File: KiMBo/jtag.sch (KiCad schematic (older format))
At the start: 9 parts, among them U1 OSD3358, Y2 6K30032768K0702070401, Y3 7A-24.000MAAJ-T

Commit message: Create more footprints and add more associations
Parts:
- Y3: footprint (none) -> KiMBo:Crystal_SMD_7A_2Pads
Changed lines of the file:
@@
 F 0 "Y3" V 4800 4150 50  0000 C CNN
 F 1 "7A-24.000MAAJ-T" V 4375 3875 50  0000 C CNN
-F 2 "" H 4700 4000 50  0001 C CNN
+F 2 "KiMBo:Crystal_SMD_7A_2Pads" H 4700 4000 50  0001 C CNN
 F 3 "" H 4700 4000 50  0000 C CNN
 	1    4700 4000

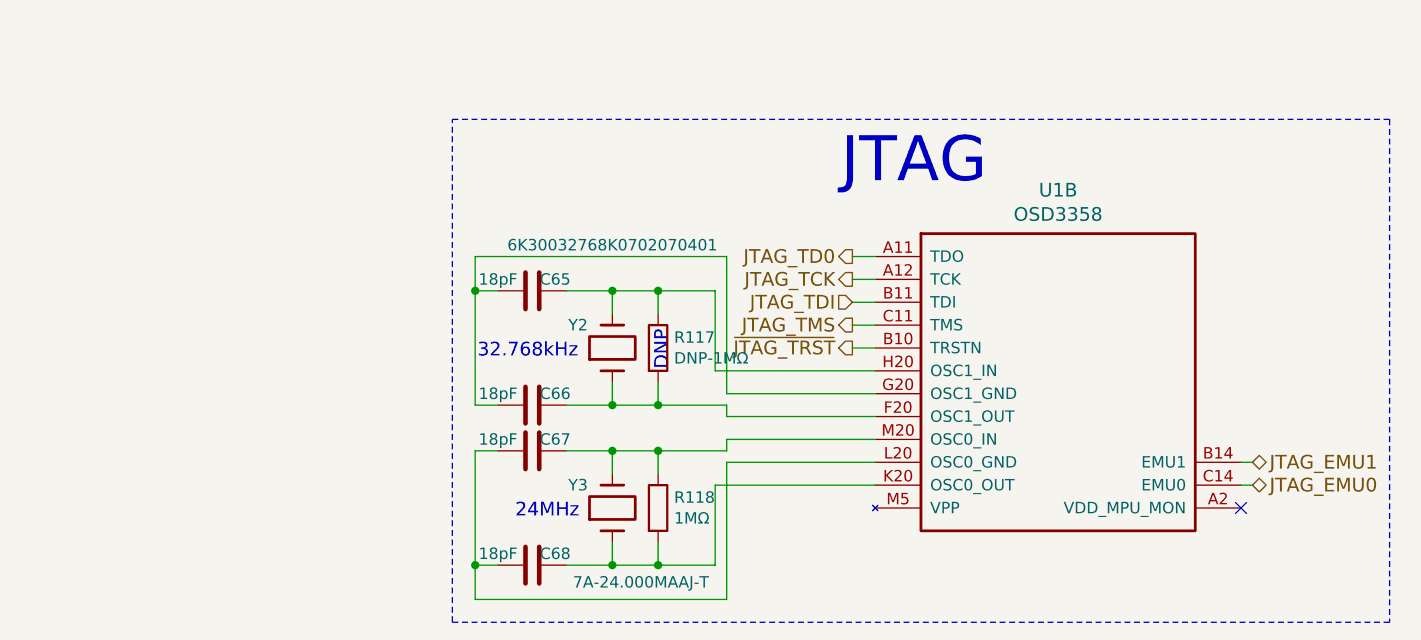
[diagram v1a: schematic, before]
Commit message: Complete footprint association
Next step is layout, adjustments may need to be made to the schematic at a later point.
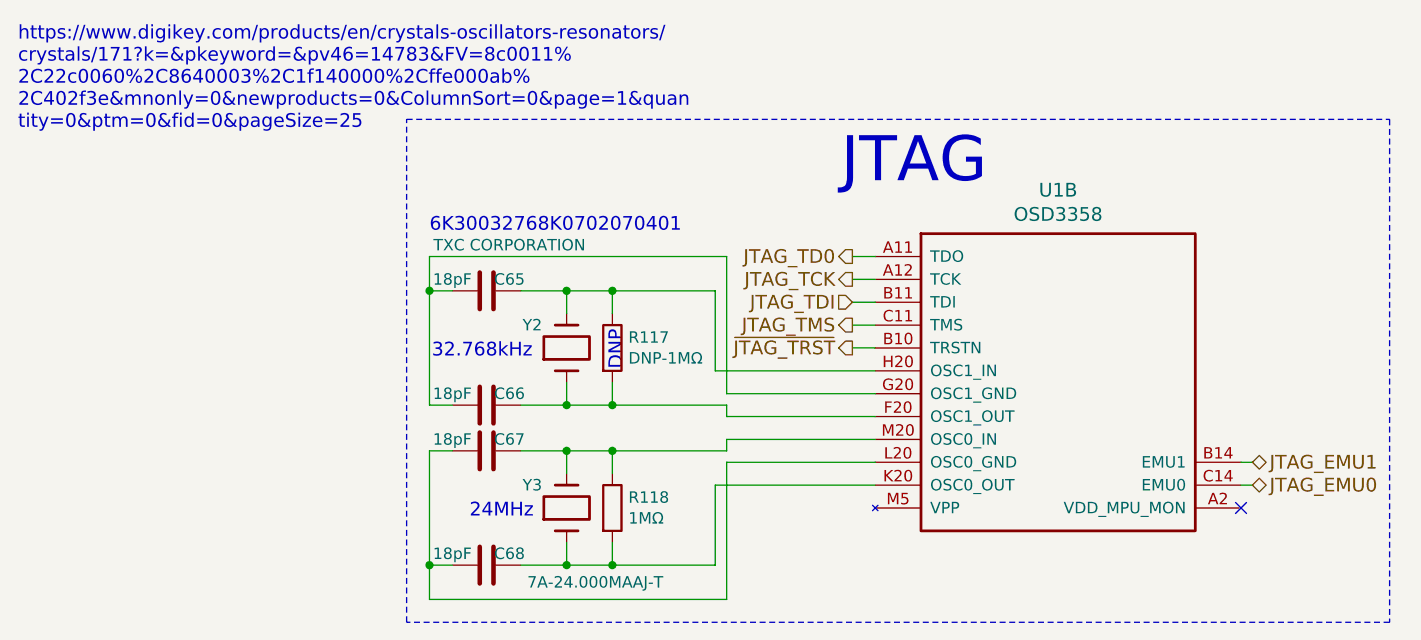
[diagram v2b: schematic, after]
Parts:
- R117: footprint (none) -> Resistors_SMD:R_0603
- Y2: value 6K30032768K0702070401 -> TXC CORPORATION; footprint (none) -> KiMBo:Crystal_SMD_32.768kHz_2Pads
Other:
- note added: "6K30032768K0702070401"
- note added: "https://www.digikey.com/products/en/crystals-oscillators-resonators/\ncrystals/171?k=&pkeyword=&pv46=14783&FV=8c0011%\n2C22c0060%2C8640003%2C1f140000%2Cffe000ab%\n2C402f3e&mnonly=0&newproducts=0&ColumnSort=0&page=1&quan\ntity=0&ptm=0&fid=0&pageSize=25"
- moved on the sheet: C65, C66, C67, C68, R117, R118, Y2, Y3
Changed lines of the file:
@@
 L R R118
 U 1 1 589C1CFA
-P 4900 4000
-F 0 "R118" H 4970 4046 50  0000 L CNN
-F 1 "1MΩ" H 4970 3955 50  0000 L CNN
-F 2 "Resistors_SMD:R_0603" V 4830 4000 50  0001 C CNN
-F 3 "" H 4900 4000 50  0000 C CNN
-	1    4900 4000
+P 4700 4000
+F 0 "R118" H 4770 4046 50  0000 L CNN
+F 1 "1MΩ" H 4770 3955 50  0000 L CNN
+F 2 "Resistors_SMD:R_0603" V 4630 4000 50  0001 C CNN
+F 3 "" H 4700 4000 50  0000 C CNN
+	1    4700 4000
 	1    0    0    -1
 $EndComp
@@
 L C C67
 U 1 1 589C1D01
-P 4350 3750
-F 0 "C67" V 4400 3850 50  0000 C CNN
-F 1 "18pF" V 4400 3600 50  0000 C CNN
-F 2 "Capacitors_SMD:C_0603" H 4350 3750 50  0001 C CNN
-F 3 "" H 4350 3750 50  0000 C CNN
-	1    4350 3750
+P 4150 3750
+F 0 "C67" V 4200 3850 50  0000 C CNN
+F 1 "18pF" V 4200 3600 50  0000 C CNN
+F 2 "Capacitors_SMD:C_0603" H 4150 3750 50  0001 C CNN
+F 3 "" H 4150 3750 50  0000 C CNN
+	1    4150 3750
 	0    1    -1   0
 $EndComp
@@
 L C C68
 U 1 1 589C1D08
-P 4350 4250
-F 0 "C68" V 4400 4350 50  0000 C CNN
-F 1 "18pF" V 4400 4100 50  0000 C CNN
-F 2 "Capacitors_SMD:C_0603" H 4350 4250 50  0001 C CNN
-F 3 "" H 4350 4250 50  0000 C CNN
-	1    4350 4250
+P 4150 4250
+F 0 "C68" V 4200 4350 50  0000 C CNN
+F 1 "18pF" V 4200 4100 50  0000 C CNN
+F 2 "Capacitors_SMD:C_0603" H 4150 4250 50  0001 C CNN
+F 3 "" H 4150 4250 50  0000 C CNN
+	1    4150 4250
 	0    1    -1   0
 $EndComp
@@
 L R R117
 U 1 1 589C1D0F
-P 4900 3300
-F 0 "R117" H 4970 3346 50  0000 L CNN
-F 1 "DNP-1MΩ" H 4970 3255 50  0000 L CNN
-F 2 "" V 4830 3300 50  0001 C CNN
-F 3 "" H 4900 3300 50  0000 C CNN
-	1    4900 3300
+P 4700 3300
+F 0 "R117" H 4770 3346 50  0000 L CNN
+F 1 "DNP-1MΩ" H 4770 3255 50  0000 L CNN
+F 2 "Resistors_SMD:R_0603" V 4630 3300 50  0001 C CNN
+F 3 "" H 4700 3300 50  0000 C CNN
+	1    4700 3300
 	1    0    0    -1
 $EndComp
@@
 L C C66
 U 1 1 589C1D16
-P 4350 3550
-F 0 "C66" V 4400 3650 50  0000 C CNN
-F 1 "18pF" V 4400 3400 50  0000 C CNN
-F 2 "Capacitors_SMD:C_0603" H 4350 3550 50  0001 C CNN
-F 3 "" H 4350 3550 50  0000 C CNN
-	1    4350 3550
+P 4150 3550
+F 0 "C66" V 4200 3650 50  0000 C CNN
+F 1 "18pF" V 4200 3400 50  0000 C CNN
+F 2 "Capacitors_SMD:C_0603" H 4150 3550 50  0001 C CNN
+F 3 "" H 4150 3550 50  0000 C CNN
+	1    4150 3550
 	0    1    -1   0
 $EndComp
@@
 L C C65
 U 1 1 589C1D1D
-P 4350 3050
-F 0 "C65" V 4400 3150 50  0000 C CNN
-F 1 "18pF" V 4400 2900 50  0000 C CNN
-F 2 "Capacitors_SMD:C_0603" H 4350 3050 50  0001 C CNN
-F 3 "" H 4350 3050 50  0000 C CNN
-	1    4350 3050
+P 4150 3050
+F 0 "C65" V 4200 3150 50  0000 C CNN
+F 1 "18pF" V 4200 2900 50  0000 C CNN
+F 2 "Capacitors_SMD:C_0603" H 4150 3050 50  0001 C CNN
+F 3 "" H 4150 3050 50  0000 C CNN
+	1    4150 3050
 	0    1    -1   0
 $EndComp
@@
 L CRYSTAL Y3
 U 1 1 589C1D2C
-P 4700 4000
-F 0 "Y3" V 4800 4150 50  0000 C CNN
-F 1 "7A-24.000MAAJ-T" V 4375 3875 50  0000 C CNN
-F 2 "KiMBo:Crystal_SMD_7A_2Pads" H 4700 4000 50  0001 C CNN
-F 3 "" H 4700 4000 50  0000 C CNN
-	1    4700 4000
+P 4500 4000
+F 0 "Y3" V 4600 4150 50  0000 C CNN
+F 1 "7A-24.000MAAJ-T" V 4175 3875 50  0000 C CNN
+F 2 "KiMBo:Crystal_SMD_7A_2Pads" H 4500 4000 50  0001 C CNN
+F 3 "" H 4500 4000 50  0000 C CNN
+	1    4500 4000
 	0    -1   -1   0
 $EndComp
@@
 L CRYSTAL Y2
 U 1 1 589C1D33
-P 4700 3300
-F 0 "Y2" V 4800 3450 50  0000 C CNN
-F 1 "6K30032768K0702070401" V 5150 3300 50  0000 C CNN
-F 2 "" H 4700 3300 50  0001 C CNN
-F 3 "" H 4700 3300 50  0000 C CNN
-	1    4700 3300
+P 4500 3300
+F 0 "Y2" V 4600 3450 50  0000 C CNN
+F 1 "TXC CORPORATION" V 4950 3550 50  0000 C CNN
+F 2 "KiMBo:Crystal_SMD_32.768kHz_2Pads" H 4500 3300 50  0001 C CNN
+F 3 "" H 4500 3300 50  0000 C CNN
+	1    4500 3300
 	0    -1   -1   0
 $EndComp
-Connection ~ 4100 4250
+Connection ~ 3900 4250
 Wire Wire Line
 	5850 3800 5200 3800
 Wire Wire Line
-	4100 4250 4200 4250
-Wire Wire Line
-	4100 3750 4100 4400
-Wire Wire Line
-	4200 3750 4100 3750
+	3900 4250 4000 4250
+Wire Wire Line
+	3900 3750 3900 4400
+Wire Wire Line
+	4000 3750 3900 3750
 Wire Wire Line
 	5150 4250 5150 3900
 Wire Wire Line
 	5150 3900 5850 3900
-Connection ~ 4900 4250
-Wire Wire Line
-	4900 4250 4900 4150
-Connection ~ 4900 3750
-Wire Wire Line
-	4900 3750 4900 3850
-Wire Notes Line
-	4000 4500 4000 2300
-Wire Notes Line
-	8100 4500 4000 4500
+Connection ~ 4700 4250
+Wire Wire Line
+	4700 4250 4700 4150
+Connection ~ 4700 3750
+Wire Wire Line
+	4700 3750 4700 3850
+Wire Notes Line
+	3800 4500 3800 2300
+Wire Notes Line
+	8100 4500 3800 4500
 Wire Notes Line
 	8100 2300 8100 4500
 Wire Notes Line
-	4000 2300 8100 2300
-Wire Wire Line
-	4100 4400 5200 4400
+	3800 2300 8100 2300
+Wire Wire Line
+	3900 4400 5200 4400
 Wire Wire Line
 	5200 4400 5200 3800
@@
 	5150 3400 5150 3050
 Wire Wire Line
-	4900 3050 4900 3150
-Connection ~ 4900 3050
-Wire Wire Line
-	4900 3550 4900 3450
-Connection ~ 4900 3550
-Wire Wire Line
-	4100 3550 4200 3550
-Wire Wire Line
-	4100 2900 4100 3550
-Wire Wire Line
-	4100 3050 4200 3050
+	4700 3050 4700 3150
+Connection ~ 4700 3050
+Wire Wire Line
+	4700 3550 4700 3450
+Connection ~ 4700 3550
+Wire Wire Line
+	3900 3550 4000 3550
+Wire Wire Line
+	3900 2900 3900 3550
+Wire Wire Line
+	3900 3050 4000 3050
 Wire Wire Line
 	5850 3500 5200 3500
@@
 	5200 3500 5200 2900
 Wire Wire Line
-	5200 2900 4100 2900
-Connection ~ 4100 3050
+	5200 2900 3900 2900
+Connection ~ 3900 3050
 Wire Wire Line
 	5850 2900 5750 2900
@@
 	7450 3900 7500 3900
 Wire Wire Line
-	5200 3550 4500 3550
-Wire Wire Line
-	5150 3050 4500 3050
-Wire Wire Line
-	4500 4250 5150 4250
-Wire Wire Line
-	4500 3750 5200 3750
-Wire Wire Line
-	4700 3850 4700 3750
-Connection ~ 4700 3750
-Wire Wire Line
-	4700 4150 4700 4250
-Connection ~ 4700 4250
-Wire Wire Line
-	4700 3150 4700 3050
-Connection ~ 4700 3050
-Wire Wire Line
-	4700 3450 4700 3550
-Connection ~ 4700 3550
+	5200 3550 4300 3550
+Wire Wire Line
+	5150 3050 4300 3050
+Wire Wire Line
+	4300 4250 5150 4250
+Wire Wire Line
+	4300 3750 5200 3750
+Wire Wire Line
+	4500 3850 4500 3750
+Connection ~ 4500 3750
+Wire Wire Line
+	4500 4150 4500 4250
+Connection ~ 4500 4250
+Wire Wire Line
+	4500 3150 4500 3050
+Connection ~ 4500 3050
+Wire Wire Line
+	4500 3450 4500 3550
+Connection ~ 4500 3550
 Text HLabel 5750 2900 0    60   Output ~ 0
 JTAG_TD0
@@
 Text HLabel 7500 3900 2    60   BiDi ~ 0
 JTAG_EMU0
-Text Notes 4950 3400 1    60   ~ 0
+Text Notes 4750 3400 1    60   ~ 0
 DNP
-Text Notes 4110 3350 0    60   ~ 0
+Text Notes 3910 3350 0    60   ~ 0
 32.768kHz
-Text Notes 4275 4050 0    60   ~ 0
+Text Notes 4075 4050 0    60   ~ 0
 24MHz
+Text Notes 2100 2350 0    60   ~ 0
+https://www.digikey.com/products/en/crystals-oscillators-resonators/\ncrystals/171?k=&pkeyword=&pv46=14783&FV=8c0011%\n2C22c0060%2C8640003%2C1f140000%2Cffe000ab%\n2C402f3e&mnonly=0&newproducts=0&ColumnSort=0&page=1&quan\ntity=0&ptm=0&fid=0&pageSize=25
+Text Notes 3900 2800 0    60   ~ 0
+6K30032768K0702070401
 $EndSCHEMATC

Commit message: Begin layout
Arrange all connectors to get a feel for the area.
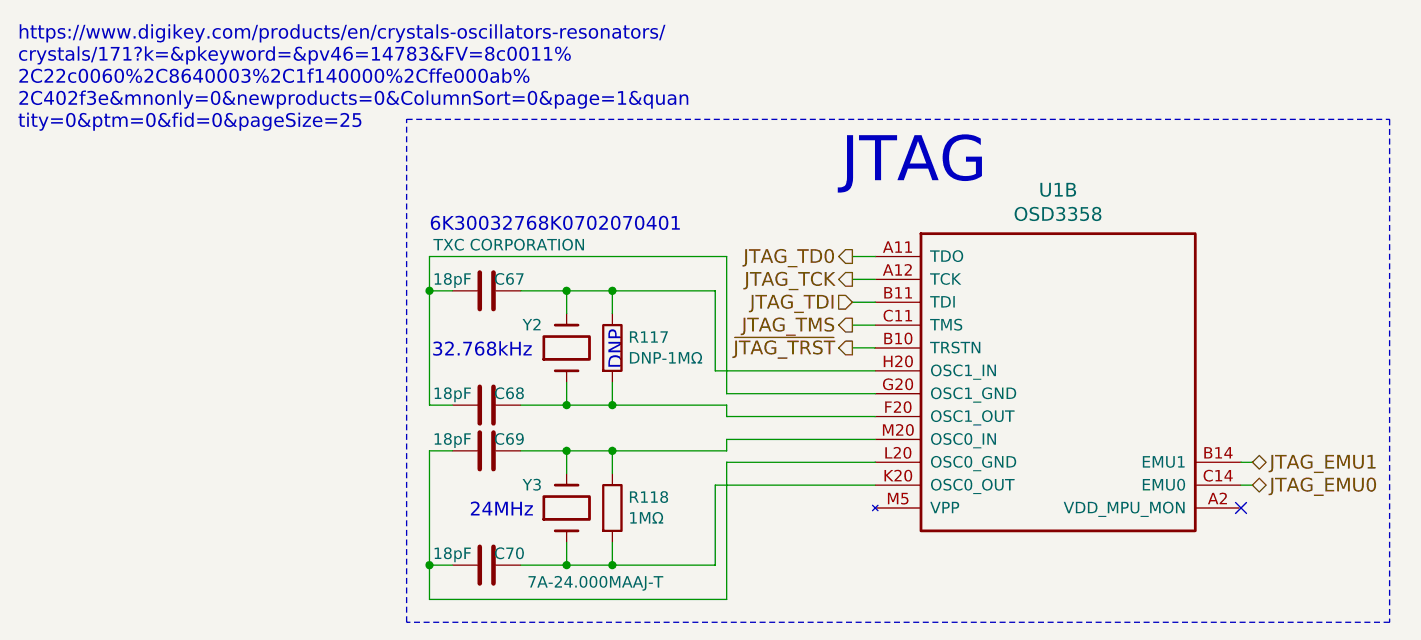
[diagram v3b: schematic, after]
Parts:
- renumbered C65 to C67, C66 to C68, C67 to C69, C68 to C70
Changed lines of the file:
@@
 $EndComp
 $Comp
-L C C67
+L C C69
 U 1 1 589C1D01
 P 4150 3750
-F 0 "C67" V 4200 3850 50  0000 C CNN
+F 0 "C69" V 4200 3850 50  0000 C CNN
 F 1 "18pF" V 4200 3600 50  0000 C CNN
 F 2 "Capacitors_SMD:C_0603" H 4150 3750 50  0001 C CNN
@@
 $EndComp
 $Comp
-L C C68
+L C C70
 U 1 1 589C1D08
 P 4150 4250
-F 0 "C68" V 4200 4350 50  0000 C CNN
+F 0 "C70" V 4200 4350 50  0000 C CNN
 F 1 "18pF" V 4200 4100 50  0000 C CNN
 F 2 "Capacitors_SMD:C_0603" H 4150 4250 50  0001 C CNN
@@
 $EndComp
 $Comp
-L C C66
+L C C68
 U 1 1 589C1D16
 P 4150 3550
-F 0 "C66" V 4200 3650 50  0000 C CNN
+F 0 "C68" V 4200 3650 50  0000 C CNN
 F 1 "18pF" V 4200 3400 50  0000 C CNN
 F 2 "Capacitors_SMD:C_0603" H 4150 3550 50  0001 C CNN
@@
 $EndComp
 $Comp
-L C C65
+L C C67
 U 1 1 589C1D1D
 P 4150 3050
-F 0 "C65" V 4200 3150 50  0000 C CNN
+F 0 "C67" V 4200 3150 50  0000 C CNN
 F 1 "18pF" V 4200 2900 50  0000 C CNN
 F 2 "Capacitors_SMD:C_0603" H 4150 3050 50  0001 C CNN

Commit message: Tune in the stepper motor circuit, prior to removing HDMI
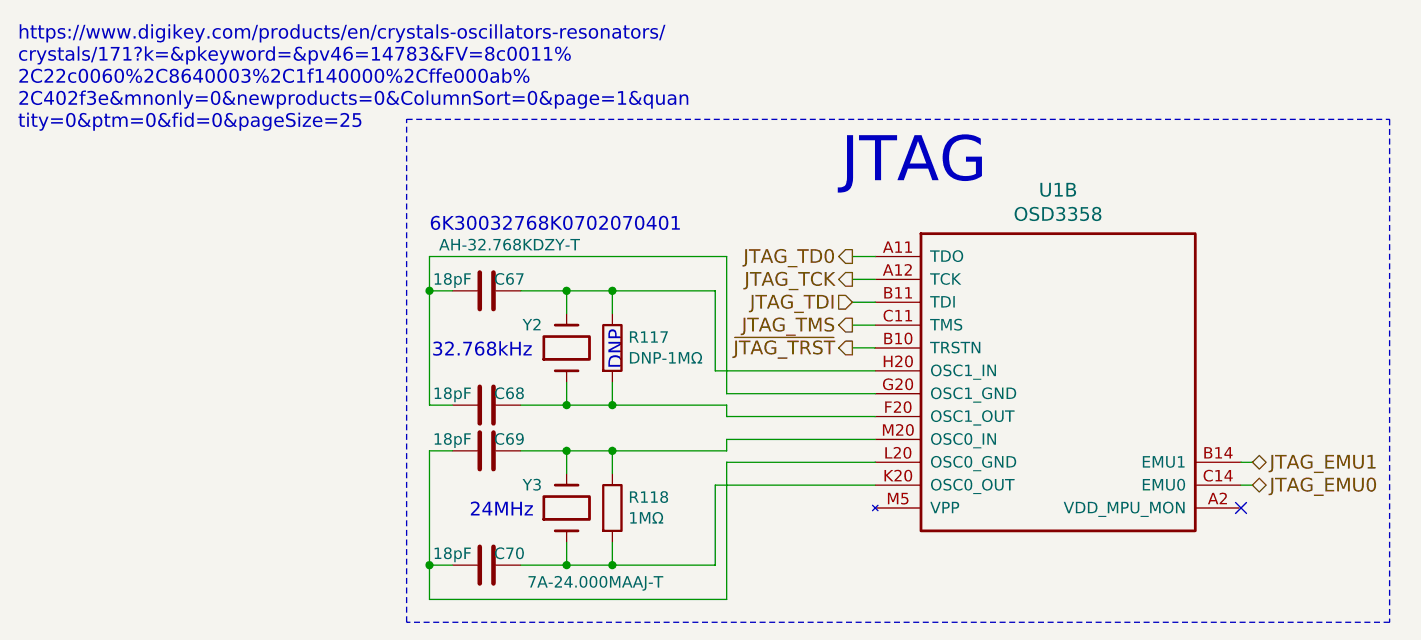
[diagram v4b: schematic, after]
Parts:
- Y2: value TXC CORPORATION -> AH-32.768KDZY-T
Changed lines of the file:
@@
 P 4500 3300
 F 0 "Y2" V 4600 3450 50  0000 C CNN
-F 1 "TXC CORPORATION" V 4950 3550 50  0000 C CNN
+F 1 "AH-32.768KDZY-T" V 4950 3550 50  0000 C CNN
 F 2 "KiMBo:Crystal_SMD_32.768kHz_2Pads" H 4500 3300 50  0001 C CNN
 F 3 "" H 4500 3300 50  0000 C CNN

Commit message: Remove HDMI from the schematic
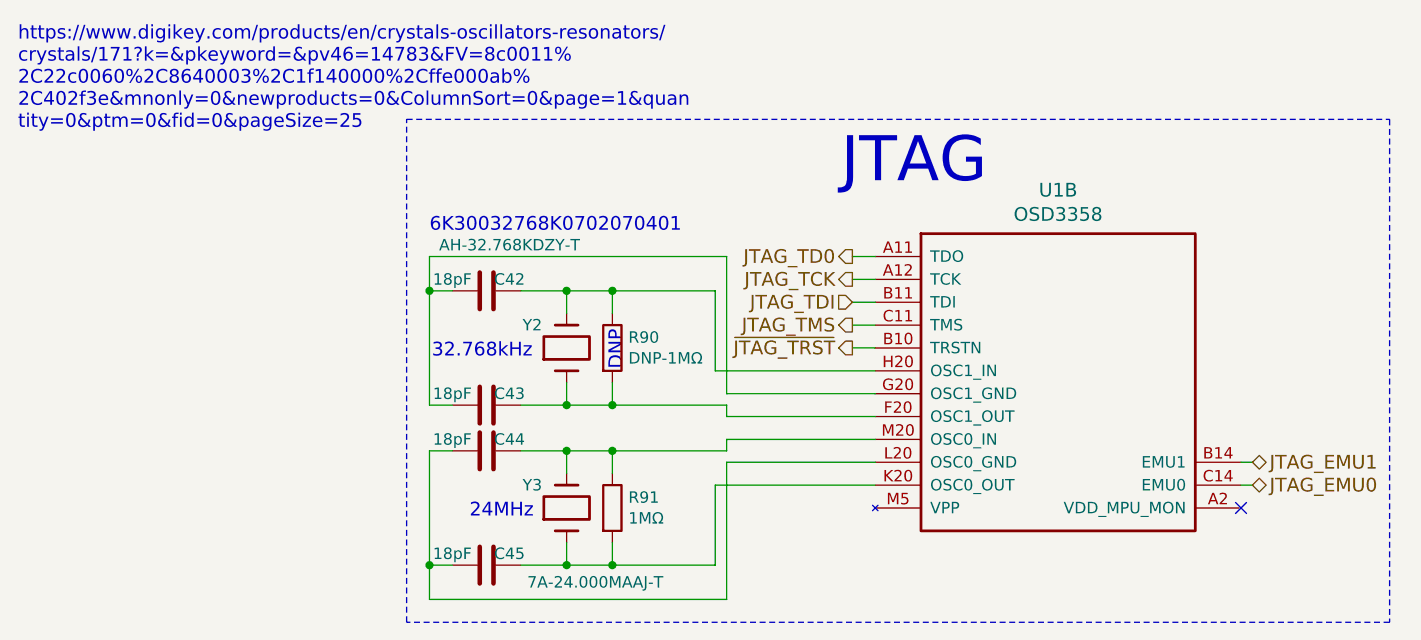
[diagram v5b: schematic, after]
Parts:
- renumbered C67 to C42, C68 to C43, C69 to C44, C70 to C45, R117 to R90, R118 to R91
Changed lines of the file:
@@
 $Descr A4 11693 8268
 encoding utf-8
-Sheet 12 26
+Sheet 12 25
 Title ""
 Date ""
@@
 JTAG
 $Comp
-L R R118
+L R R91
 U 1 1 589C1CFA
 P 4700 4000
-F 0 "R118" H 4770 4046 50  0000 L CNN
+F 0 "R91" H 4770 4046 50  0000 L CNN
 F 1 "1MΩ" H 4770 3955 50  0000 L CNN
 F 2 "Resistors_SMD:R_0603" V 4630 4000 50  0001 C CNN
@@
 $EndComp
 $Comp
-L C C69
+L C C44
 U 1 1 589C1D01
 P 4150 3750
-F 0 "C69" V 4200 3850 50  0000 C CNN
+F 0 "C44" V 4200 3850 50  0000 C CNN
 F 1 "18pF" V 4200 3600 50  0000 C CNN
 F 2 "Capacitors_SMD:C_0603" H 4150 3750 50  0001 C CNN
@@
 $EndComp
 $Comp
-L C C70
+L C C45
 U 1 1 589C1D08
 P 4150 4250
-F 0 "C70" V 4200 4350 50  0000 C CNN
+F 0 "C45" V 4200 4350 50  0000 C CNN
 F 1 "18pF" V 4200 4100 50  0000 C CNN
 F 2 "Capacitors_SMD:C_0603" H 4150 4250 50  0001 C CNN
@@
 $EndComp
 $Comp
-L R R117
+L R R90
 U 1 1 589C1D0F
 P 4700 3300
-F 0 "R117" H 4770 3346 50  0000 L CNN
+F 0 "R90" H 4770 3346 50  0000 L CNN
 F 1 "DNP-1MΩ" H 4770 3255 50  0000 L CNN
 F 2 "Resistors_SMD:R_0603" V 4630 3300 50  0001 C CNN
@@
 $EndComp
 $Comp
-L C C68
+L C C43
 U 1 1 589C1D16
 P 4150 3550
-F 0 "C68" V 4200 3650 50  0000 C CNN
+F 0 "C43" V 4200 3650 50  0000 C CNN
 F 1 "18pF" V 4200 3400 50  0000 C CNN
 F 2 "Capacitors_SMD:C_0603" H 4150 3550 50  0001 C CNN
@@
 $EndComp
 $Comp
-L C C67
+L C C42
 U 1 1 589C1D1D
 P 4150 3050
-F 0 "C67" V 4200 3150 50  0000 C CNN
+F 0 "C42" V 4200 3150 50  0000 C CNN
 F 1 "18pF" V 4200 2900 50  0000 C CNN
 F 2 "Capacitors_SMD:C_0603" H 4150 3050 50  0001 C CNN
